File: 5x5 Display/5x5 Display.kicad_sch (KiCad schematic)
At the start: 52 parts, among them U3 DRV1

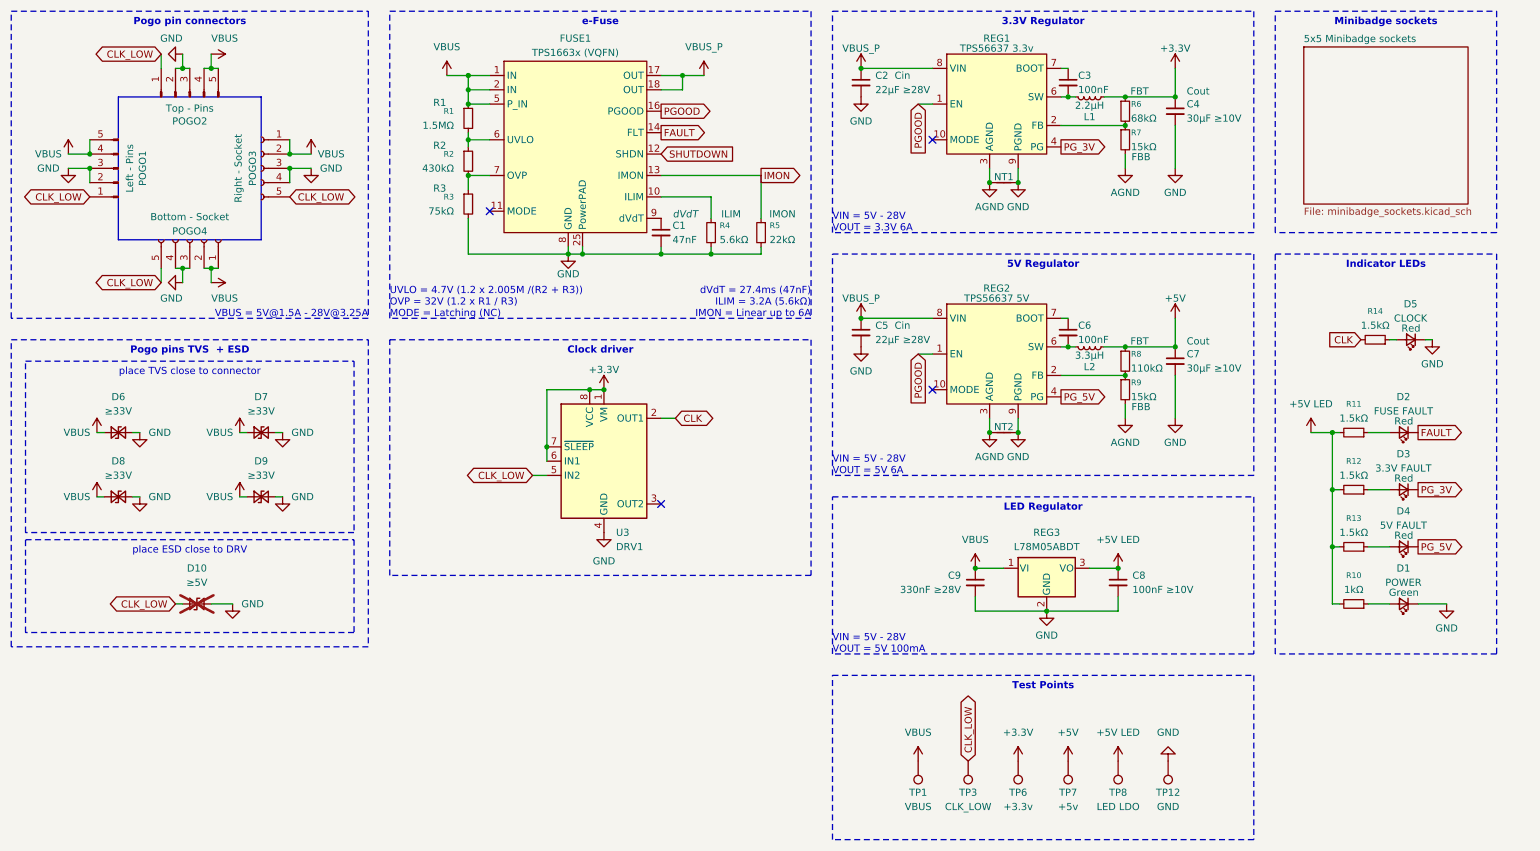
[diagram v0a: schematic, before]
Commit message: R2 initial commit
* remove eFuse
* remove LED regulator
* swap bucks for cheaper ones
* add reverse polarity
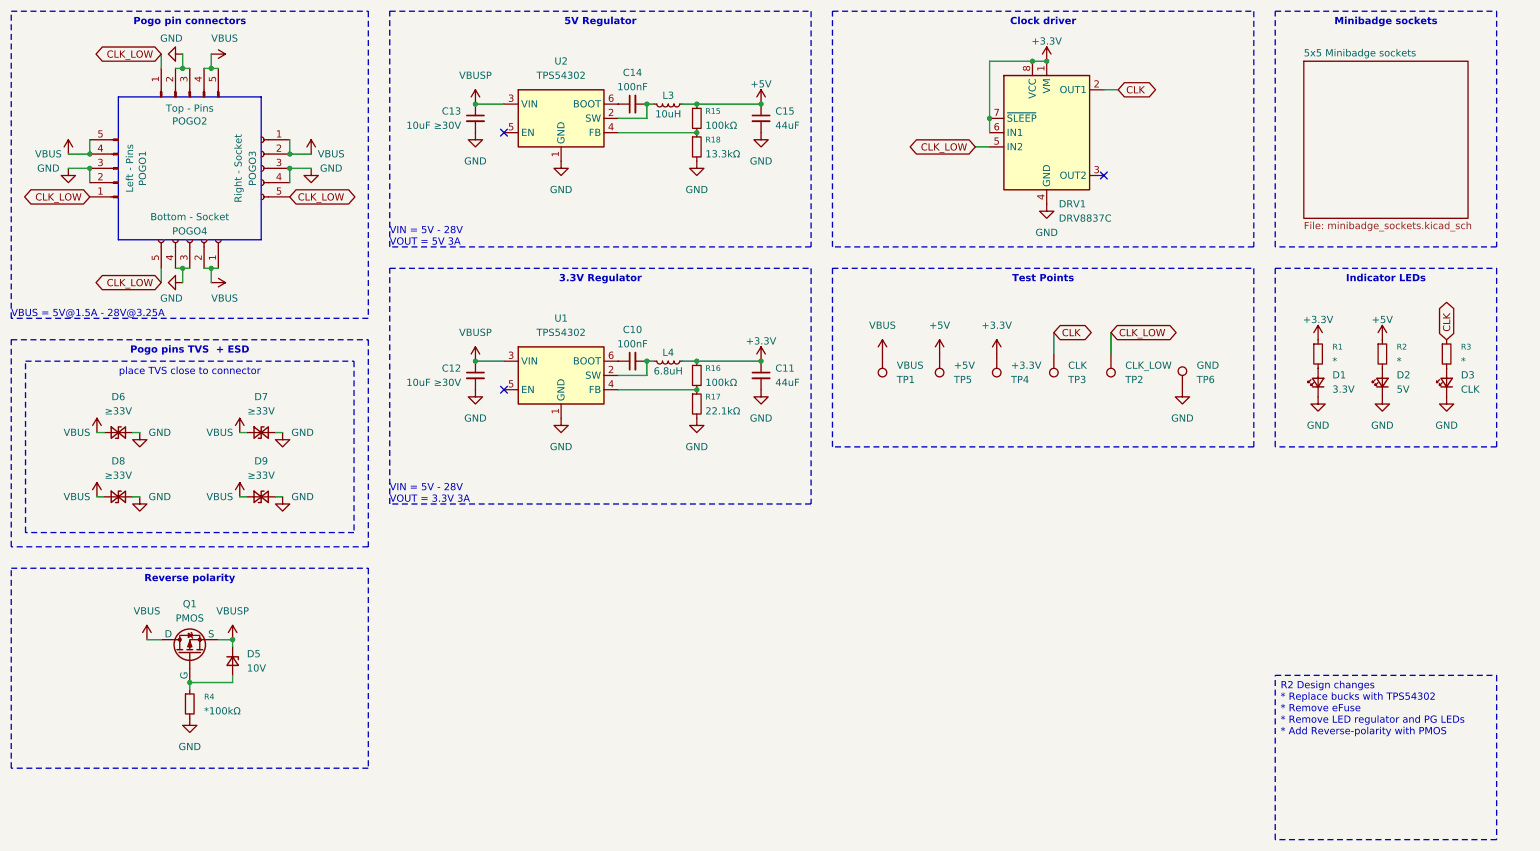
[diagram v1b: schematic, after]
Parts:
- removed C1: 47nF, Capacitor_SMD:C_0603_1608Metric, symbol Device:C_Small
- removed C2, C5: 22μF ≥28V, Capacitor_SMD:C_1206_3216Metric, symbol Device:C_Small
- removed C3, C6: 100nF, Capacitor_SMD:C_0603_1608Metric, symbol Device:C_Small
- removed C4, C7: 30μF ≥10V, Capacitor_SMD:C_1206_3216Metric, symbol Device:C_Small
- removed C8: 100nF ≥10V, Capacitor_SMD:C_0603_1608Metric, symbol Device:C_Small
- removed C9: 330nF ≥28V, Capacitor_SMD:C_0805_2012Metric, symbol Device:C_Small
- removed D10: ≥5V, Diode_SMD:D_SOD-323, symbol Device:D_TVS_Small
- removed D4: 5V FAULT, LED_SMD:LED_0805_2012Metric, symbol Device:LED_Small
- removed D5: CLOCK, LED_SMD:LED_0805_2012Metric, symbol Device:LED_Small
- removed FUSE1: TPS1663x (VQFN), Package_DFN_QFN:VQFN-24-1EP_4x4mm_P0.5mm_EP2.5x2.5mm_ThermalVias, symbol TPS1663x:TPS1663x VQFN
- removed L1: 2.2μH, Inductor_SMD:L_6.3x6.3_H3, symbol Device:L_Small
- removed L2: 3.3μH, Inductor_SMD:L_6.3x6.3_H3, symbol Device:L_Small
- removed NT1, NT2: NT, NetTie:NetTie-2_SMD_Pad0.5mm, symbol Device:NetTie_2
- removed R10: 1kΩ, Resistor_SMD:R_0603_1608Metric, symbol Device:R_Small
- removed R11, R12, R13, R14: 1.5kΩ, Resistor_SMD:R_0603_1608Metric, symbol Device:R_Small
- removed R5: 22kΩ, Resistor_SMD:R_0603_1608Metric, symbol Device:R_Small
- removed R6: 68kΩ, Resistor_SMD:R_0603_1608Metric, symbol Device:R_Small
- removed R7, R9: 15kΩ, Resistor_SMD:R_0603_1608Metric, symbol Device:R_Small
- removed R8: 110kΩ, Resistor_SMD:R_0603_1608Metric, symbol Device:R_Small
- removed REG1: TPS56637 3.3v, TPS56637:TPS56637 VQFN-HR (10), symbol TPS56637:TPS56637
- removed REG2: TPS56637 5V, TPS56637:TPS56637 VQFN-HR (10), symbol TPS56637:TPS56637
- removed REG3: L78M05ABDT, Package_TO_SOT_SMD:TO-252-2, symbol Regulator_Linear:KA78M05_TO252
- removed TP12: GND, TestPoint:TestPoint_Pad_D1.5mm, symbol Connector:TestPoint
- removed TP7: +5v, TestPoint:TestPoint_Pad_D1.5mm, symbol Connector:TestPoint
- removed TP8: LED LDO, TestPoint:TestPoint_Pad_D1.5mm, symbol Connector:TestPoint
- added C10, C14: 100nF, symbol Device:C_Small
- added C11, C15: 44uF, symbol Device:C_Small
- added C12, C13: 10uF ≥30V, symbol Device:C_Small
- added D5: 10V, symbol Device:D_Zener_Small
- added L3: 10uH, symbol Device:L_Small
- added L4: 6.8uH, symbol Device:L_Small
- added Q1: PMOS, symbol Simulation_SPICE:PMOS
- added R15, R16: 100kΩ, symbol Device:R_Small
- added R17: 22.1kΩ, symbol Device:R_Small
- added R18: 13.3kΩ, symbol Device:R_Small
- added TP2: CLK_LOW, symbol Connector:TestPoint
- added TP4: +3.3V, symbol Connector:TestPoint
- added TP5: +5V, symbol Connector:TestPoint
- added U1, U2: TPS54302, Package_TO_SOT_SMD:SOT-23-6, symbol Regulator_Switching:TPS54302
- D1: value POWER -> 3.3V; footprint LED_SMD:LED_0805_2012Metric -> (none); LCSC Part # C2297 -> (none); Name Green -> (none)
- D2: value FUSE FAULT -> 5V; footprint LED_SMD:LED_0805_2012Metric -> (none); LCSC Part # C84256 -> (none); Name Red -> (none)
- D3: value 3.3V FAULT -> CLK; footprint LED_SMD:LED_0805_2012Metric -> (none); LCSC Part # C84256 -> (none); Name Red -> (none)
- DRV1: renamed from U3; value DRV1 -> DRV8837C
- R1: value 1.5MΩ -> *; footprint Resistor_SMD:R_0603_1608Metric -> (none); LCSC Part # C4172 -> (none); Name R1 -> (none)
- R2: value 430kΩ -> *; footprint Resistor_SMD:R_0603_1608Metric -> (none); LCSC Part # C25969 -> (none); Name R2 -> (none)
- R3: value 75kΩ -> *; footprint Resistor_SMD:R_0603_1608Metric -> (none); LCSC Part # C23242 -> (none); Name R3 -> (none)
- R4: value 5.6kΩ -> *100kΩ; footprint Resistor_SMD:R_0603_1608Metric -> (none); LCSC Part # C23189 -> (none); Name ILIM -> (none)
- TP1: footprint TestPoint:TestPoint_Pad_D1.5mm -> (none); now in the parts list
- TP3: value CLK_LOW -> CLK; footprint TestPoint:TestPoint_Pad_D1.5mm -> (none); now in the parts list
- TP6: value +3.3v -> GND; footprint TestPoint:TestPoint_Pad_D1.5mm -> (none); now in the parts list
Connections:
- net FAULT is gone; now on net GND: D2.1 (K)
- net PG_3V is gone; now on net GND: D3.1 (K)
- net +3.3V: now also R1.1, C11.1, L4.2, R16.1, TP4.1; no longer TP6.1
- net +5V: now also R2.1, C15.1, L3.2, R15.1, TP5.1
- net CLK: now also R3.1, TP3.1
- net CLK_LOW: now also TP2.1; no longer TP3.1
- net GND: now also TP6.1, C11.2, C12.2, C13.2, C15.2, R17.2, R18.2, U1.1 (GND), U2.1 (GND); no longer R3.2
- net VBUS: now also Q1.1 (D); no longer R1.1
- net at R4.1: now also D5.2 (A), Q1.2 (G)
- net at D1.2 (A): now also R1.2
- net at R2.2: now also D2.2 (A); no longer R3.1
- net at D3.2 (A): now also R3.2
- new net: C14.2, L3.1, U2.2 (SW)
- new net: R15.2, R18.1, U2.4 (FB)
- new net: C10.1, U1.6 (BOOT)
- new net: C10.2, L4.1, U1.2 (SW)
- new net: C14.1, U2.6 (BOOT)
- new net: R16.2, R17.1, U1.4 (FB)
- new net VBUSP: C12.1, C13.1, D5.1 (K), Q1.3 (S), U1.3 (VIN), U2.3 (VIN)
- no-connect marks 4 -> 3
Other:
- note added: "VIN = 5V - 28V VOUT = 3.3V 3A"
- note added: "VIN = 5V - 28V VOUT = 5V 3A"
- note removed: "UVLO = 4.7V (1.2 x 2.005M /(R2 + R3)) OVP = 32V (1.2 x R1 / R3) MODE = Latching (NC)"
- note removed: "VIN = 5V - 28V VOUT = 3.3V 6A"
- note removed: "VIN = 5V - 28V VOUT = 5V 100mA"
- note removed: "VIN = 5V - 28V VOUT = 5V 6A"
- note removed: "dVdT = 27.4ms (47nF) ILIM = 3.2A (5.6kΩ) IMON = Linear up to 6A"
- moved on the sheet: DRV1

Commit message: R2
R2 changes
- Reverse polarity protection
- clamp voltage on CLK_BUS
- cheaper regulators
- removal of eFuse (will be upstream on PD module)
- removal of Power Good architecture
- removal of housekeeping regulator and indicators
- re-design of test points and indicator LEDs.
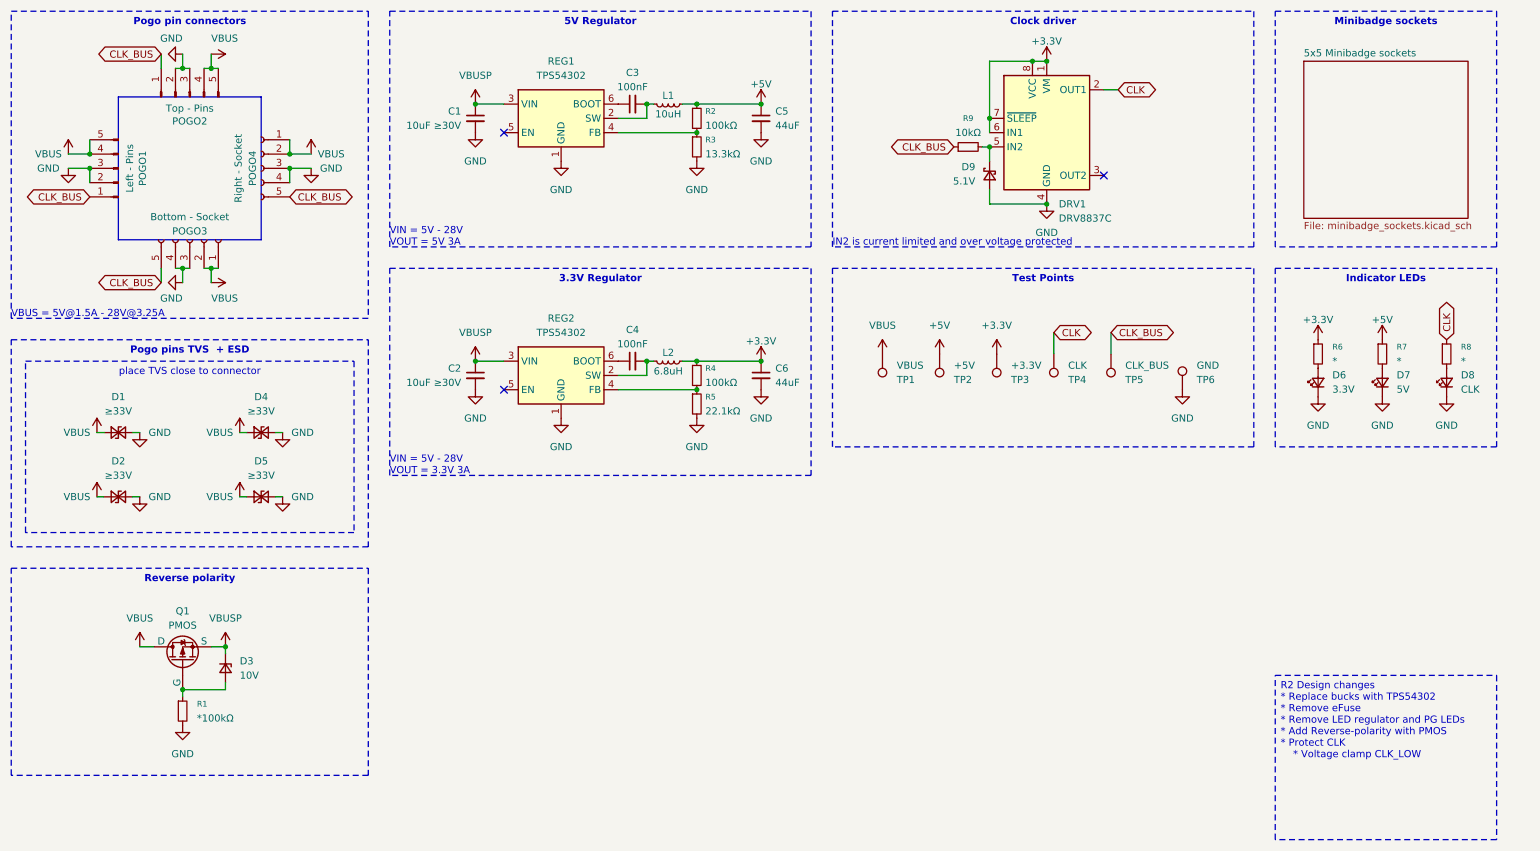
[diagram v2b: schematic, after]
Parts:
- added D9: 5.1V, symbol Device:D_Schottky_Small
- added R9: 10kΩ, symbol Device:R_Small
- C1: renamed from C13; footprint (none) -> Capacitor_SMD:C_1206_3216Metric
- C2: renamed from C12; footprint (none) -> Capacitor_SMD:C_1206_3216Metric
- C3: renamed from C14; footprint (none) -> Capacitor_SMD:C_0805_2012Metric
- C4: renamed from C10; footprint (none) -> Capacitor_SMD:C_0805_2012Metric
- C5: renamed from C15; footprint (none) -> Capacitor_SMD:C_1206_3216Metric
- C6: renamed from C11; footprint (none) -> Capacitor_SMD:C_1206_3216Metric
- D3: renamed from D5; footprint (none) -> LED_SMD:LED_0805_2012Metric
- D6: renamed from D1; footprint (none) -> Capacitor_SMD:C_0805_2012Metric
- D7: renamed from D2; footprint (none) -> LED_SMD:LED_0805_2012Metric
- D8: renamed from D3; footprint (none) -> LED_SMD:LED_0805_2012Metric
- L1: renamed from L3; footprint (none) -> Inductor_SMD:L_TechFuse_SL0630
- L2: renamed from L4; footprint (none) -> Inductor_SMD:L_TechFuse_SL0630
- R1: renamed from R4; footprint (none) -> Resistor_SMD:R_0805_2012Metric
- R2: renamed from R15; footprint (none) -> Resistor_SMD:R_0805_2012Metric
- R3: renamed from R18; footprint (none) -> Resistor_SMD:R_0805_2012Metric
- R4: renamed from R16; footprint (none) -> Resistor_SMD:R_0805_2012Metric
- R5: renamed from R17; footprint (none) -> Resistor_SMD:R_0805_2012Metric
- R6: renamed from R1; footprint (none) -> Resistor_SMD:R_0805_2012Metric
- R7: renamed from R2; footprint (none) -> Resistor_SMD:R_0805_2012Metric
- R8: renamed from R3; footprint (none) -> Resistor_SMD:R_0805_2012Metric
- TP1, TP6: footprint (none) -> TestPoint:TestPoint_Pad_D1.5mm; now left out of the parts list
- TP2: renamed from TP5; footprint (none) -> TestPoint:TestPoint_Pad_D1.5mm; now left out of the parts list
- TP3: renamed from TP4; footprint (none) -> TestPoint:TestPoint_Pad_D1.5mm; now left out of the parts list
- TP4: renamed from TP3; footprint (none) -> TestPoint:TestPoint_Pad_D1.5mm; now left out of the parts list
- TP5: renamed from TP2; value CLK_LOW -> CLK_BUS; footprint (none) -> TestPoint:TestPoint_Pad_D1.5mm; now left out of the parts list
- renumbered D6 to D1, D8 to D2, D7 to D4, D9 to D5, POGO4 to POGO3, POGO3 to POGO4, U2 to REG1, U1 to REG2
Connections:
- net GND: now also D9.2 (A)
- net CLK_LOW renamed CLK_BUS
- net CLK_BUS: now also R9.1; no longer DRV1.5 (IN2)
- new net: D9.1 (K), DRV1.5 (IN2), R9.2
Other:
- note added: "IN2 is current limited and over voltage protected"
- company: Pips Engineering -> Beehive Engineering
- moved on the sheet: D3, Q1, R1

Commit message: R2 updates
* Component selection and footprint finished
* Added feed-forward capacitor
* Increased capacitance for Cin
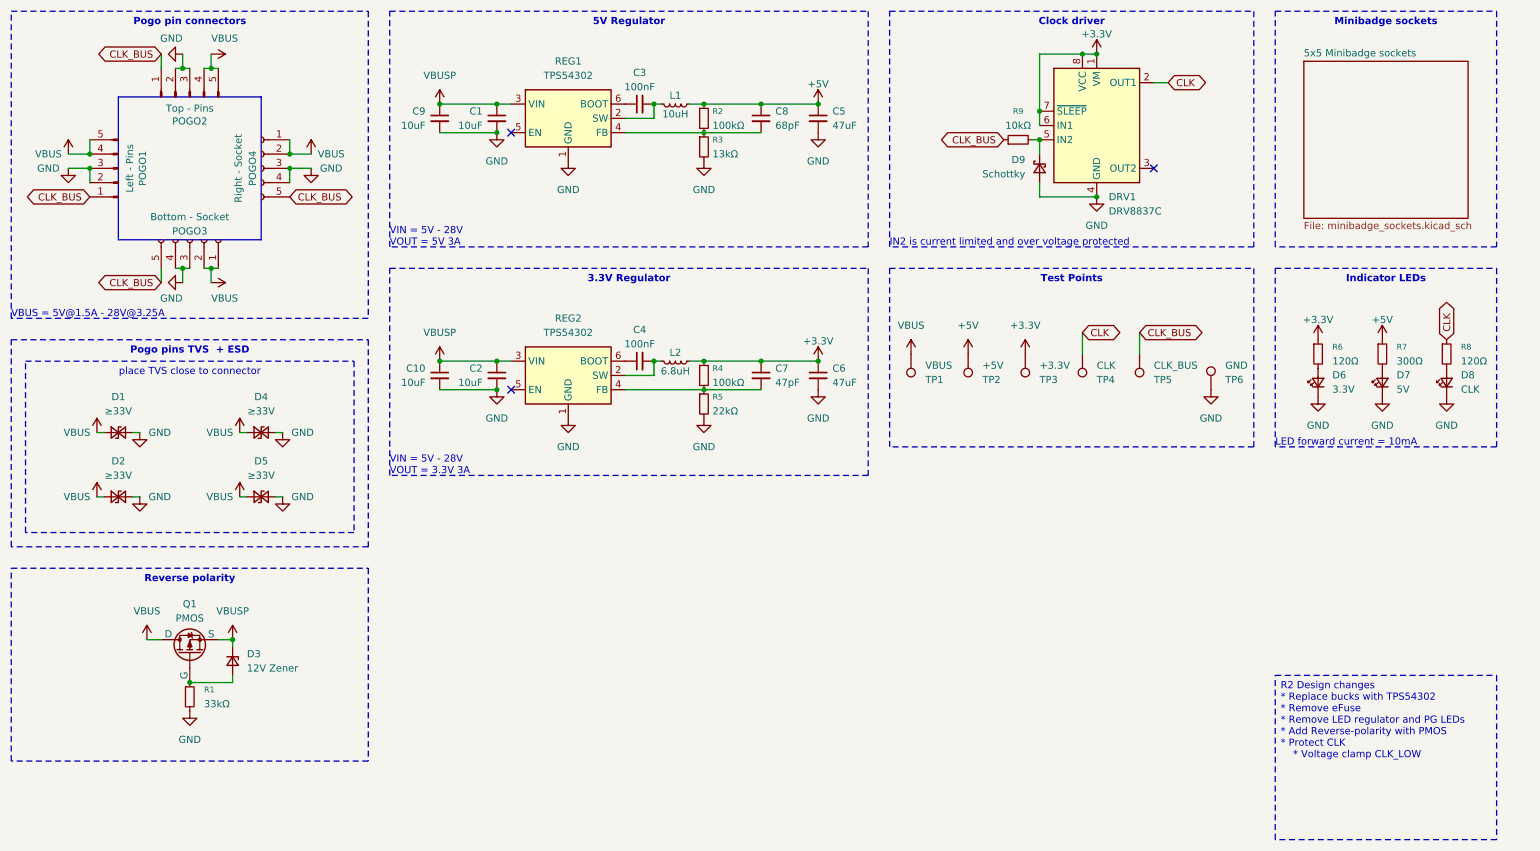
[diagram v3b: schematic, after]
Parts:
- added C10, C9: 10uF, Capacitor_SMD:C_1206_3216Metric, symbol Device:C_Small
- added C7: 47pF, Capacitor_SMD:C_0603_1608Metric, symbol Device:C_Small
- added C8: 68pF, Capacitor_SMD:C_0603_1608Metric, symbol Device:C_Small
- C1, C2: value 10uF ≥30V -> 10uF; LCSC Part # (none) -> C13585
- C3, C4: LCSC Part # (none) -> C24497
- C5, C6: value 44uF -> 47uF; LCSC Part # (none) -> C96123
- D3: value 10V -> 12V Zener; footprint LED_SMD:LED_0805_2012Metric -> Diode_SMD:D_SOD-123; LCSC Part # (none) -> C22435092
- D6: footprint Capacitor_SMD:C_0805_2012Metric -> LED_SMD:LED_0805_2012Metric; LCSC Part # (none) -> C84256
- D7: LCSC Part # (none) -> C84256
- D8: LCSC Part # (none) -> C96123
- D9: value 5.1V -> Schottky; footprint (none) -> Diode_SMD:D_SOD-123; LCSC Part # (none) -> C7420325
- Q1: footprint (none) -> Package_DFN_QFN:PQFN-8-EP_6x5mm_P1.27mm_Generic; LCSC Part # (none) -> C51625746
- R1: value *100kΩ -> 33kΩ
- R2, R4: LCSC Part # (none) -> C149504
- R3: value 13.3kΩ -> 13kΩ; LCSC Part # (none) -> C17455
- R5: value 22.1kΩ -> 22kΩ; LCSC Part # (none) -> C17560
- R6, R8: value * -> 120Ω; LCSC Part # (none) -> C17437
- R7: value * -> 300Ω; LCSC Part # (none) -> C17617
- R9: footprint (none) -> Resistor_SMD:R_0805_2012Metric; LCSC Part # (none) -> C17414
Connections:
- net +3.3V: now also C7.1
- net +5V: now also C8.1
- net GND: now also C10.2, C9.2
- net VBUS: now also Q1.5 (D), Q1.6 (D), Q1.7 (D), Q1.8 (D), Q1.9 (D); no longer Q1.1 (D)
- net VBUSP: now also Q1.1 (S), Q1.2 (S), C10.1, C9.1
- net at R2.2, R3.1, REG1.4 (FB): now also C8.2
- net at D3.2 (A), R1.1: now also Q1.4 (G); no longer Q1.2 (G)
- net at R4.2, R5.1, REG2.4 (FB): now also C7.2
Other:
- note added: "LED forward current = 10mA"
- moved on the sheet: C1, C2, C3, C4, C5, C6, D3, D9, DRV1, L1, L2, Q1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
